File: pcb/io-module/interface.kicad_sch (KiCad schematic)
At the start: 33 parts

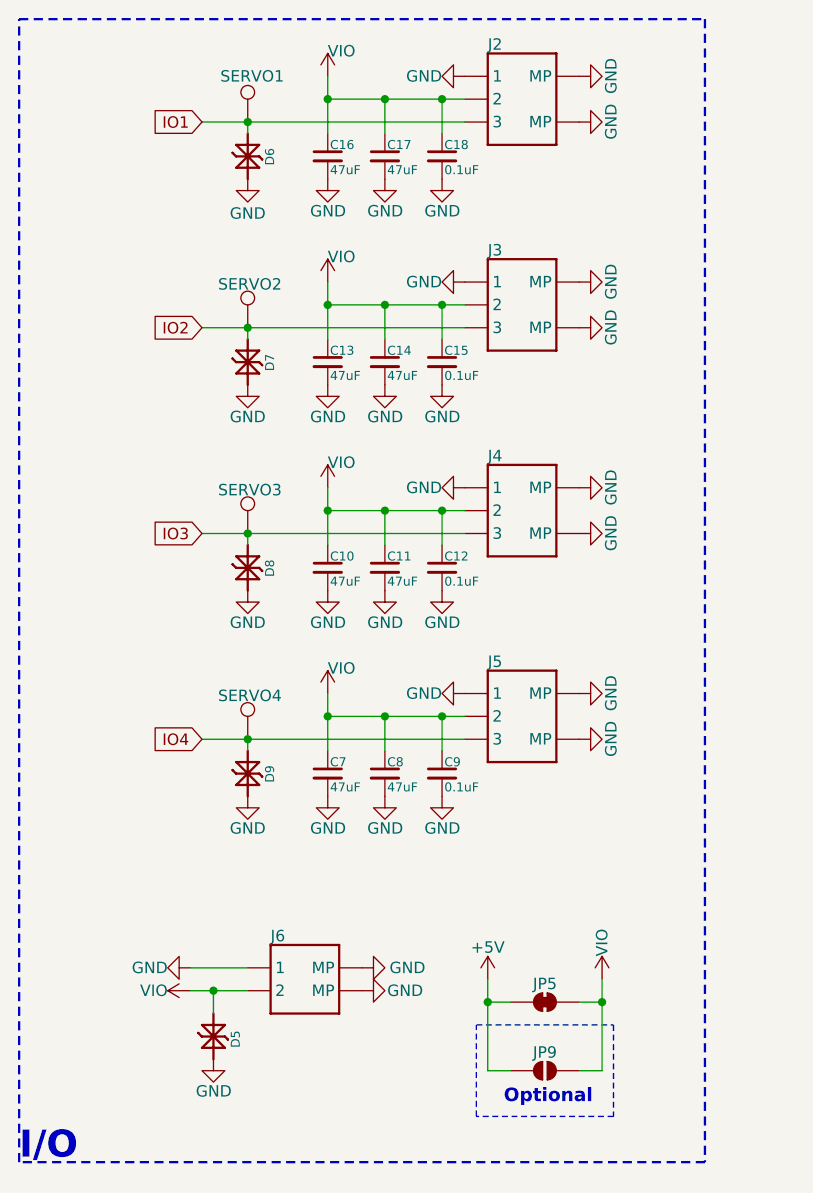
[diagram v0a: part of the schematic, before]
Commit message: Updated parts and IO power connection
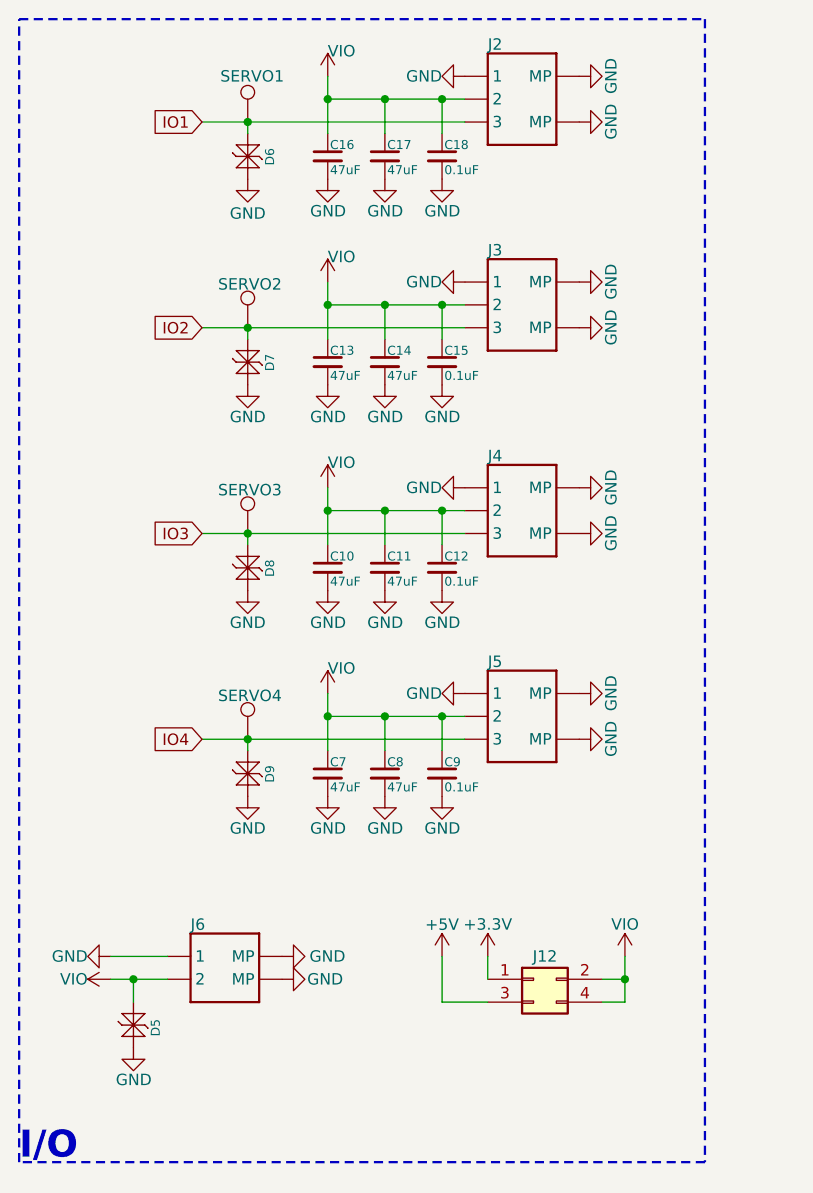
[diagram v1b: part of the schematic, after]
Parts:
- removed JP5: (no value), CRGM Connector:SolderJumper-2_P2.0mm_Bridged_RoundedPad1.0x1.5mm, symbol Jumper:SolderJumper_2_Bridged
- removed JP9: (no value), CRGM Connector:SolderJumper-2_P1.3mm_Open_RoundedPad1.0x1.5mm, symbol CRGM Connector:SolderJumper_2_Open
- added J12: Conn_02x02_Odd_Even, CRGM Connector:PinHeader_2x02_P1.27mm_Vertical_SMD, symbol Connector_Generic:Conn_02x02_Odd_Even
- D5: MN TECH PUBLIC -> Nexperia; MPN TPSP3022-01ETG -> PESD5V5C1BLYL
- D6, D7, D8, D9: MN FUXINSEMI -> (none); MPN LESD8D3.3CAT5G -> (none)
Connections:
- net +3.3V: now also J12.1 (Pin_1)
- net +5V: now also J12.3 (Pin_3)
- net VIO: now also J12.2 (Pin_2), J12.4 (Pin_4)
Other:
- note removed: "Optional"
- moved on the sheet: D5, J6
